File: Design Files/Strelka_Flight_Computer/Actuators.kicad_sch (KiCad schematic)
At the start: 16 parts, among them Q3 AO3401A, Q4 AP2300, Q5 AO3401A, Q6 AP2300, Q7 AO3401A, Q8 AP2300, U6 LM358

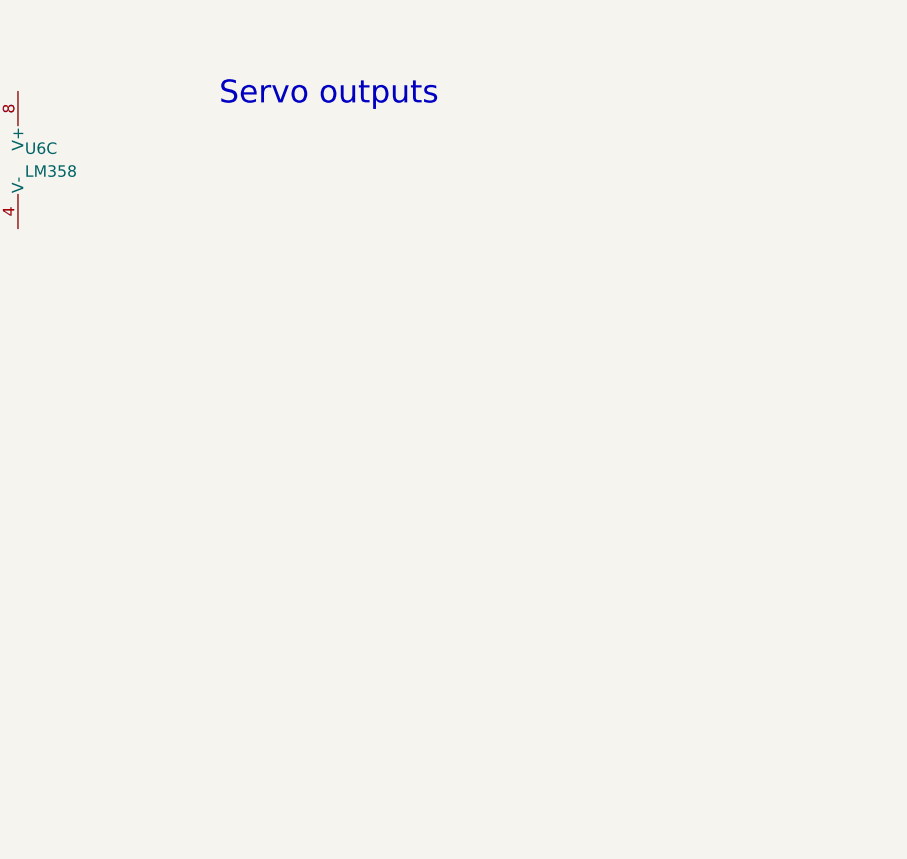
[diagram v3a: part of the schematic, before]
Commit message: Added power board, almost finished Strelka schematic
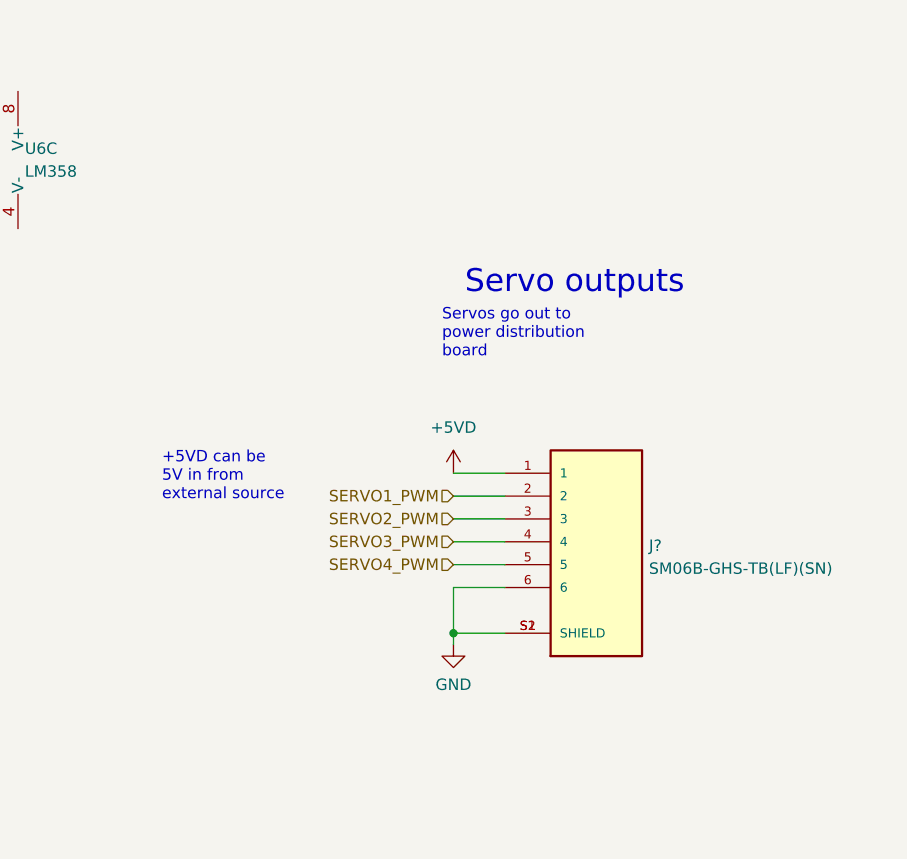
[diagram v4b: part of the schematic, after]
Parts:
- added J?: SM06B-GHS-TB(LF)(SN), Footprints:JST_SM06B-GHS-TB(LF)(SN), symbol SM06B-GHS-TB_LF__SN_:SM06B-GHS-TB(LF)(SN)
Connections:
- net GND: now also J?.6, J?.S1 (SHIELD), J?.S2 (SHIELD)
- new net +5VD: J?.1
- new net SERVO1_PWM: J?.2
- new net SERVO2_PWM: J?.3
- new net SERVO3_PWM: J?.4
- new net SERVO4_PWM: J?.5
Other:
- note added: "+5VD can be 5V in from external source"
- note added: "Servos go out to power distribution board"
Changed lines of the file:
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@@
 (kicad_sch (version 20211123) (generator eeschema)
   (paper "A4")
+  (junction (at 220.345 102.87) (diameter 0) (color 0 0 0 0)
+  )
+  (wire (pts (xy 220.345 90.17) (xy 226.06 90.17))
+    (stroke (width 0) (type default) (color 0 0 0 0))
+  )
   (wire (pts (xy 74.93 107.315) (xy 77.47 107.315))
     (stroke (width 0) (type default) (color 0 0 0 0))
@@
     (stroke (width 0) (type default) (color 0 0 0 0))
   )
+  (wire (pts (xy 220.345 102.87) (xy 220.345 104.14))
+    (stroke (width 0) (type default) (color 0 0 0 0))
+  )
   (wire (pts (xy 67.31 101.6) (xy 67.31 102.235))
     (stroke (width 0) (type default) (color 0 0 0 0))
   )
+  (wire (pts (xy 220.345 85.09) (xy 226.06 85.09))
+    (stroke (width 0) (type default) (color 0 0 0 0))
+  )
+  (wire (pts (xy 220.345 97.79) (xy 226.06 97.79))
+    (stroke (width 0) (type default) (color 0 0 0 0))
+  )
   (wire (pts (xy 82.55 151.13) (xy 84.455 151.13))
     (stroke (width 0) (type default) (color 0 0 0 0))
@@
     (stroke (width 0) (type default) (color 0 0 0 0))
   )
+  (wire (pts (xy 220.345 87.63) (xy 226.06 87.63))
+    (stroke (width 0) (type default) (color 0 0 0 0))
+  )
   (wire (pts (xy 82.55 120.015) (xy 84.455 120.015))
     (stroke (width 0) (type default) (color 0 0 0 0))
@@
     (stroke (width 0) (type default) (color 0 0 0 0))
   )
+  (wire (pts (xy 226.06 102.87) (xy 220.345 102.87))
+    (stroke (width 0) (type default) (color 0 0 0 0))
+  )
   (wire (pts (xy 45.72 71.755) (xy 67.31 71.755))
     (stroke (width 0) (type default) (color 0 0 0 0))
   )
+  (wire (pts (xy 220.345 97.79) (xy 220.345 102.87))
+    (stroke (width 0) (type default) (color 0 0 0 0))
+  )
   (wire (pts (xy 82.55 76.835) (xy 84.455 76.835))
     (stroke (width 0) (type default) (color 0 0 0 0))
   )
+  (wire (pts (xy 220.345 92.71) (xy 226.06 92.71))
+    (stroke (width 0) (type default) (color 0 0 0 0))
+  )
   (wire (pts (xy 74.93 76.835) (xy 77.47 76.835))
     (stroke (width 0) (type default) (color 0 0 0 0))
@@
     (stroke (width 0) (type default) (color 0 0 0 0))
   )
+  (wire (pts (xy 220.345 95.25) (xy 226.06 95.25))
+    (stroke (width 0) (type default) (color 0 0 0 0))
+  )
   (wire (pts (xy 82.55 107.315) (xy 84.455 107.315))
     (stroke (width 0) (type default) (color 0 0 0 0))
@@
     (effects (font (size 1.27 1.27)) (justify left bottom))
   )
+  (text "+5VD can be\n5V in from \nexternal source" (at 187.96 88.265 0)
+    (effects (font (size 1.27 1.27)) (justify left bottom))
+  )
   (text "To connector" (at 31.75 71.12 0)
     (effects (font (size 1.27 1.27)) (justify left bottom))
   )
-  (text "Servo outputs" (at 194.31 44.45 0)
+  (text "Servo outputs" (at 221.615 65.405 0)
     (effects (font (size 2.54 2.54)) (justify left bottom))
+  )
+  (text "Servos go out to \npower distribution \nboard" (at 219.075 72.39 0)
+    (effects (font (size 1.27 1.27)) (justify left bottom))
   )
   (text "To connector" (at 31.75 158.115 0)
@@
     (effects (font (size 1.27 1.27)) (justify right))
   )
+  (hierarchical_label "SERVO1_PWM" (shape input) (at 220.345 87.63 180)
+    (effects (font (size 1.27 1.27)) (justify right))
+  )
   (hierarchical_label "DROGUE_H" (shape input) (at 84.455 107.315 0)
     (effects (font (size 1.27 1.27)) (justify left))
@@
     (effects (font (size 1.27 1.27)) (justify left))
   )
+  (hierarchical_label "SERVO4_PWM" (shape input) (at 220.345 95.25 180)
+    (effects (font (size 1.27 1.27)) (justify right))
+  )
   (hierarchical_label "AUX-" (shape input) (at 50.8 158.75 270)
     (effects (font (size 1.27 1.27)) (justify right))
@@
   (hierarchical_label "MAIN+" (shape input) (at 50.165 69.215 90)
     (effects (font (size 1.27 1.27)) (justify left))
+  )
+  (hierarchical_label "SERVO3_PWM" (shape input) (at 220.345 92.71 180)
+    (effects (font (size 1.27 1.27)) (justify right))
+  )
+  (hierarchical_label "SERVO2_PWM" (shape input) (at 220.345 90.17 180)
+    (effects (font (size 1.27 1.27)) (justify right))
   )
   (hierarchical_label "AUX+" (shape input) (at 50.8 156.21 90)
@@
     (pin "1")
   )
+  (symbol (lib_id "power:+5VD") (at 220.345 85.09 0) (unit 1)
+    (in_bom yes) (on_board yes) (fields_autoplaced)
+    (property "Reference" "#PWR?" (id 0) (at 220.345 88.9 0)
+      (effects (font (size 1.27 1.27)) hide)
+    )
+    (property "Value" "+5VD" (id 1) (at 220.345 80.01 0))
+    (property "Footprint" "" (id 2) (at 220.345 85.09 0)
+      (effects (font (size 1.27 1.27)) hide)
+    )
+    (property "Datasheet" "" (id 3) (at 220.345 85.09 0)
+      (effects (font (size 1.27 1.27)) hide)
+    )
+    (pin "1")
+  )
   (symbol (lib_id "Transistor_FET:AO3401A") (at 69.85 151.13 180) (unit 1)
     (in_bom yes) (on_board yes) (fields_autoplaced)
@@
     (pin "2")
   )
+  (symbol (lib_id "SM06B-GHS-TB_LF__SN_:SM06B-GHS-TB(LF)(SN)") (at 236.22 92.71 0) (unit 1)
+    (in_bom yes) (on_board yes) (fields_autoplaced)
+    (property "Reference" "J?" (id 0) (at 242.062 93.1453 0)
+      (effects (font (size 1.27 1.27)) (justify left))
+    )
+    (property "Value" "SM06B-GHS-TB(LF)(SN)" (id 1) (at 242.062 95.6822 0)
+      (effects (font (size 1.27 1.27)) (justify left))
+    )
+    (property "Footprint" "Footprints:JST_SM06B-GHS-TB(LF)(SN)" (id 2) (at 236.22 92.71 0)
+      (effects (font (size 1.27 1.27)) (justify left bottom) hide)
+    )
+    (property "Datasheet" "" (id 3) (at 236.22 92.71 0)
+      (effects (font (size 1.27 1.27)) (justify left bottom) hide)
+    )
+    (property "PARTREV" "N/A" (id 4) (at 236.22 92.71 0)
+      (effects (font (size 1.27 1.27)) (justify left bottom) hide)
+    )
+    (property "STANDARD" "Manufacturer Recommendations" (id 5) (at 236.22 92.71 0)
+      (effects (font (size 1.27 1.27)) (justify left bottom) hide)
+    )
+    (property "MAXIMUM_PACKAGE_HEIGHT" "4.25mm" (id 6) (at 236.22 92.71 0)
+      (effects (font (size 1.27 1.27)) (justify left bottom) hide)
+    )
+    (property "MANUFACTURER" "JST" (id 7) (at 236.22 92.71 0)
+      (effects (font (size 1.27 1.27)) (justify left bottom) hide)
+    )
+    (pin "1")
+    (pin "2")
+    (pin "3")
+    (pin "4")
+    (pin "5")
+    (pin "6")
+    (pin "S1")
+    (pin "S2")
+  )
   (symbol (lib_id "Device:R_Small") (at 80.01 76.835 90) (unit 1)
     (in_bom yes) (on_board yes) (fields_autoplaced)
@@
     (pin "2")
   )
+  (symbol (lib_id "power:GND") (at 220.345 104.14 0) (unit 1)
+    (in_bom yes) (on_board yes) (fields_autoplaced)
+    (property "Reference" "#PWR?" (id 0) (at 220.345 110.49 0)
+      (effects (font (size 1.27 1.27)) hide)
+    )
+    (property "Value" "GND" (id 1) (at 220.345 108.5834 0))
+    (property "Footprint" "" (id 2) (at 220.345 104.14 0)
+      (effects (font (size 1.27 1.27)) hide)
+    )
+    (property "Datasheet" "" (id 3) (at 220.345 104.14 0)
+      (effects (font (size 1.27 1.27)) hide)
+    )
+    (pin "1")
+  )
   (symbol (lib_id "power:GND") (at 67.31 126.365 0) (unit 1)

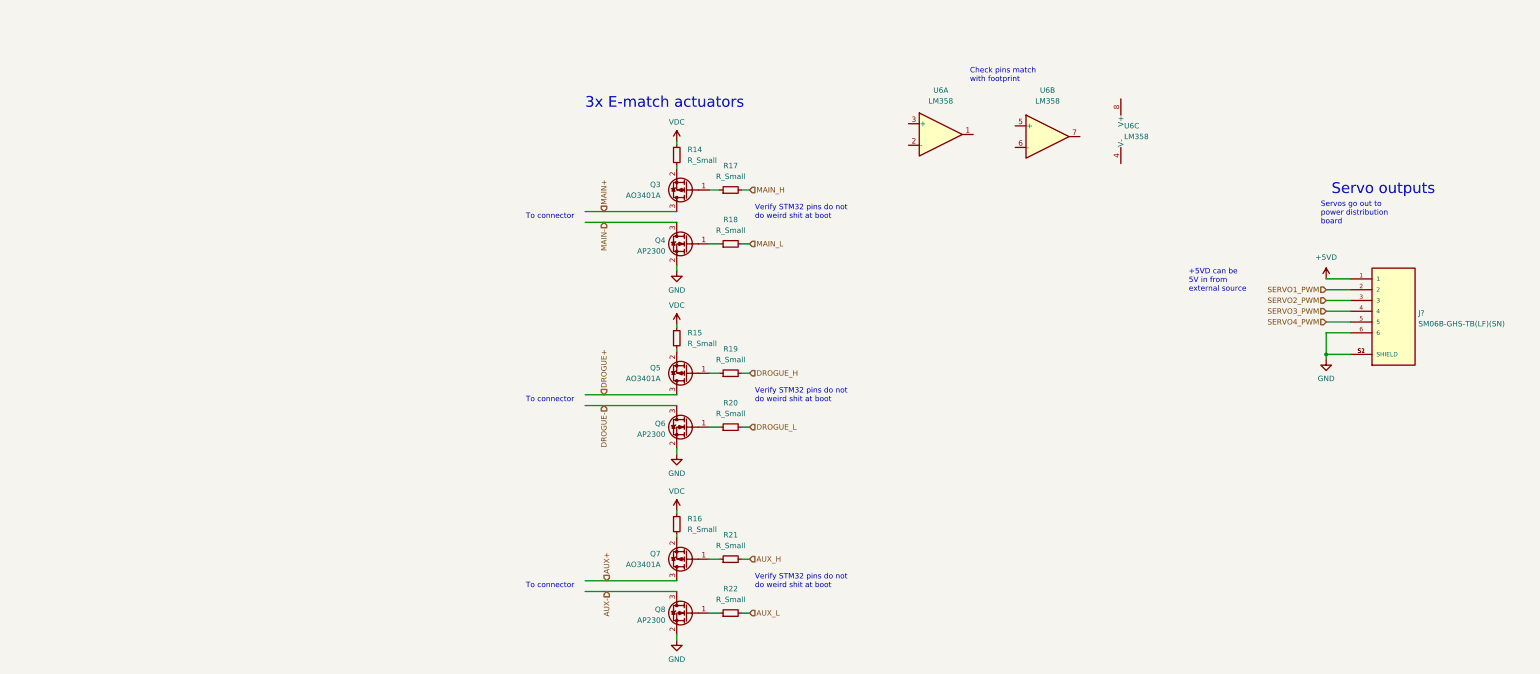
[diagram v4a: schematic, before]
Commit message: Added to continuity circuit
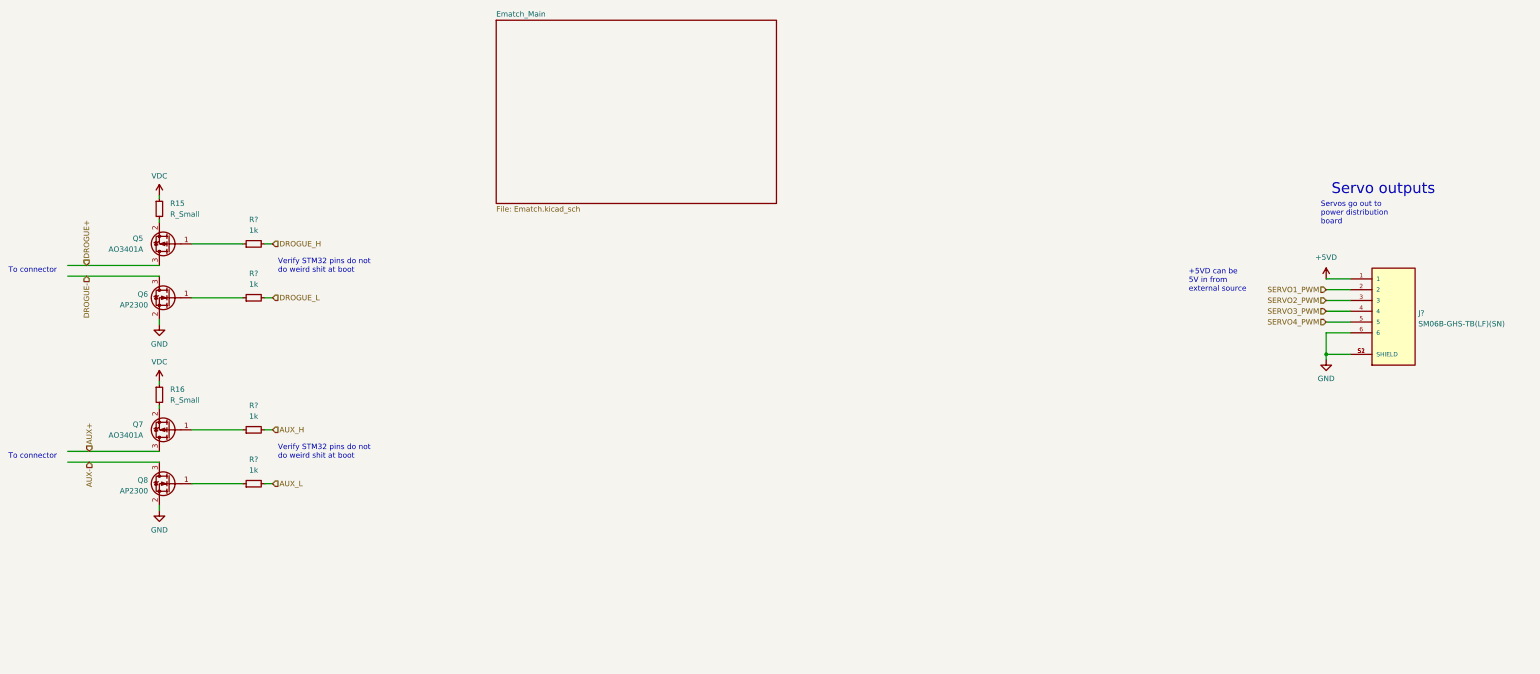
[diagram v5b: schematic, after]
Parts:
- removed Q3: AO3401A, Package_TO_SOT_SMD:SOT-23, symbol Transistor_FET:AO3401A
- removed Q4: AP2300, Package_TO_SOT_SMD:SOT-23, symbol Transistor_FET:2N7002E
- removed R14, R17, R18, R19, R20, R21, R22: R_Small, symbol Device:R_Small
- removed U6: LM358, Footprints:SOP65P490X110-8N, symbol Amplifier_Operational:LM358
- added R? (x4): 1k, Resistor_SMD:R_0603_1608Metric, symbol Device:R_Small
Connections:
- net AUX_H: now also R?.2
- net AUX_L: now also R?.2
- net DROGUE_H: now also R?.2
- net DROGUE_L: now also R?.2
- net at Q7.1 (G): now also R?.1
- net at Q6.1 (G): now also R?.1
- net at Q5.1 (G): now also R?.1
- net at Q8.1 (G): now also R?.1
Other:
- added sheet Ematch_Main (Ematch.kicad_sch)
- note removed: "3x E-match actuators"
- note removed: "Check pins match with footprint"
- moved on the sheet: Q5, Q6, Q7, Q8, R15, R16

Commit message: Added motor driver to power board
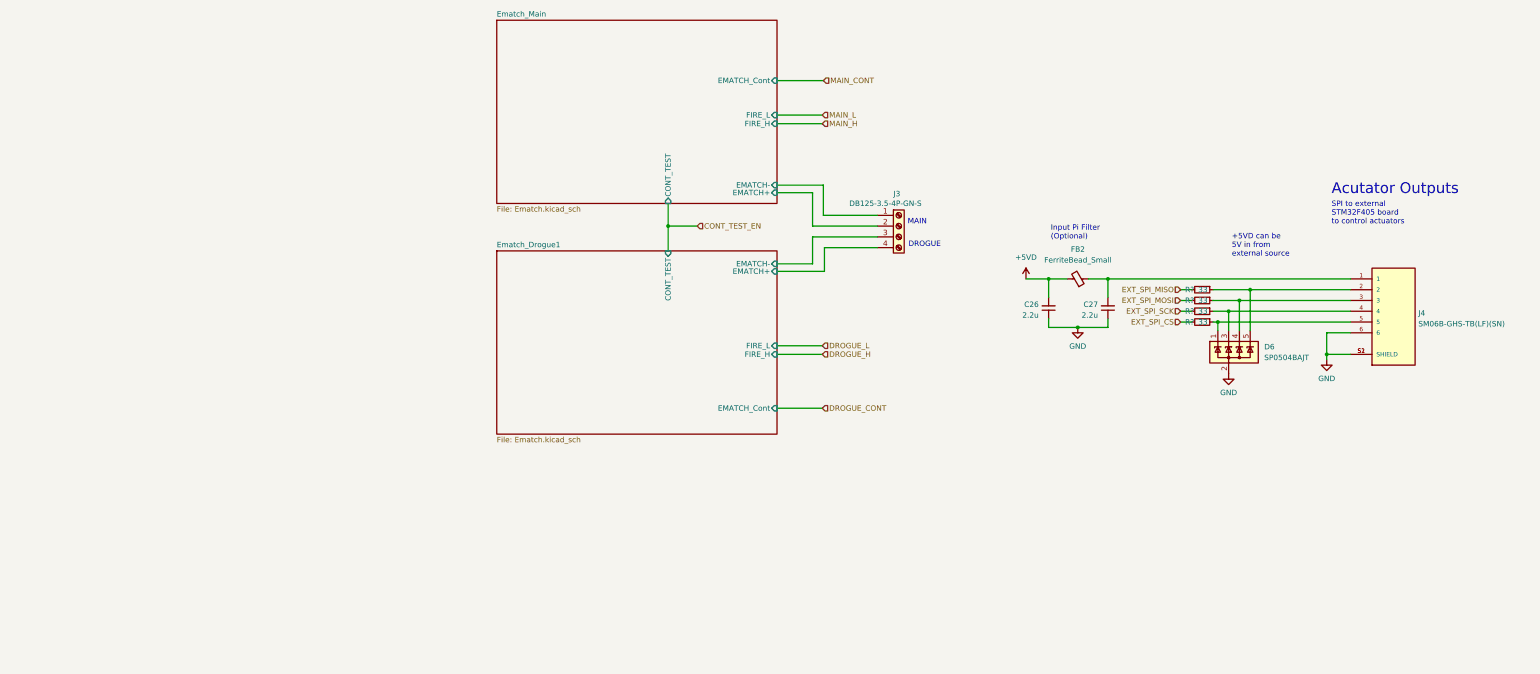
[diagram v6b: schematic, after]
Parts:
- removed Q5, Q7: AO3401A, Package_TO_SOT_SMD:SOT-23, symbol Transistor_FET:AO3401A
- removed Q6, Q8: AP2300, Package_TO_SOT_SMD:SOT-23, symbol Transistor_FET:2N7002E
- removed R15, R16: R_Small, symbol Device:R_Small
- removed R? (x4): 1k, Resistor_SMD:R_0603_1608Metric, symbol Device:R_Small
- added C26, C27: 2.2u, Capacitor_SMD:C_0603_1608Metric, symbol Device:C_Small
- added D6: SP0504BAJT, Package_TO_SOT_SMD:SOT-353_SC-70-5, symbol Power_Protection:SP0504BAJT
- added FB2: FerriteBead_Small, Inductor_SMD:L_0603_1608Metric, symbol Device:FerriteBead_Small
- added J3: DB125-3.5-4P-GN-S, TerminalBlock_4Ucon:TerminalBlock_4Ucon_1x04_P3.50mm_Horizontal, symbol Connector:Screw_Terminal_01x04
- added R? (x4): 33, Resistor_SMD:R_0603_1608Metric_Pad0.98x0.95mm_HandSolder, symbol Device:R_Small
- gave numbers to parts that had none: 1
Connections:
- net +5VD: now also C26.2, FB2.2; no longer J4.1
- net GND: now also C26.1, C27.1, D6.2 (A)
- net SERVO1_PWM: no longer names the net of J4.2
- net SERVO1_PWM: now also D6.5 (K), R?.1
- net SERVO2_PWM: no longer names the net of J4.3
- net SERVO2_PWM: now also D6.4 (K), R?.1
- net SERVO3_PWM: no longer names the net of J4.4
- net SERVO3_PWM: now also D6.3 (K), R?.1
- net SERVO4_PWM: no longer names the net of J4.5
- net SERVO4_PWM: now also D6.1 (K), R?.1
- new net: C27.2, FB2.1, J4.1
- new net EXT_SPI_CS: R?.2
- new net EXT_SPI_MISO: R?.2
- new net EXT_SPI_MOSI: R?.2
- new net EXT_SPI_SCK: R?.2
- new net Ematch_Drogue1/EMATCH+: J3.4 (Pin_4)
- new net Ematch_Drogue1/EMATCH-: J3.3 (Pin_3)
- new net Ematch_Main/EMATCH+: J3.2 (Pin_2)
- new net Ematch_Main/EMATCH-: J3.1 (Pin_1)
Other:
- added sheet Ematch_Drogue1 (Ematch.kicad_sch)
- sheet Ematch_Main ports: added CONT_TEST, EMATCH+, EMATCH-, EMATCH_Cont, FIRE_H, FIRE_L; removed none
- note added: "Acutator Outputs"
- note added: "DROGUE"
- note added: "Input Pi Filter (Optional)"
- note added: "MAIN"
- note added: "SPI to external STM32F405 board to control actuators"
- note removed: "Servo outputs"
- note removed: "Servos go out to power distribution board"
- note removed: "To connector"
- note removed: "Verify STM32 pins do not do weird shit at boot"
